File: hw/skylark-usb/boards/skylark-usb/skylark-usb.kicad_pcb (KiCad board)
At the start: 4 copper layers, 90 x 100 mm, 121 parts, among them J1 USB4105-GF-A, J2 BM08B-GHS-TBT, J3 20021111-00010T4LF, Q1 MMBFJ177LT1G, Q2 MMBFJ177LT1G, Q3 MMBFJ177LT1G, Q4 MMBFJ177LT1G, Q5 2N7002/HAMR, Q6 2N7002/HAMR, Q7 2N7002/HAMR, SW1 TL3342F160QG, SW2 TL3342F160QG, U1 STM32F072CBT6, U10 OPA387DBVR, U11 SHT40-AD1F-R2, U12 BMP390, U13 TPS22918DBVR, U2 AP2112K-3.3TRG1, U3 TPS2553DBVR, U4 REF3025AIDBZR, U5 OPA387DBVR, U6 ADS122C04IPWR, U7 OPA2387DGKR, U8 OPA387DBVR, U9 OPA2387DGKR

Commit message: Harden Skylark signal chain and add manufacturing audit
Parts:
- added C80: 100nF, Skylark:Capacitor_SMD__C_1206_3216Metric, B.Cu at (110.0, 85.5)
- added C81: 100nF, Skylark:Capacitor_SMD__C_1206_3216Metric, B.Cu at (110.0, 88.0)
- added C82: 100nF, Skylark:Capacitor_SMD__C_1206_3216Metric, B.Cu at (110.0, 90.5)
- added C83: 100nF, Skylark:Capacitor_SMD__C_1206_3216Metric, B.Cu at (110.0, 93.0)
- added C84: 100nF, Skylark:Capacitor_SMD__C_1206_3216Metric, B.Cu at (124.5, 81.5)
- added C85: 100nF, Skylark:Capacitor_SMD__C_1206_3216Metric, B.Cu at (124.5, 84.0)
- added C86: 100nF, Skylark:Capacitor_SMD__C_1206_3216Metric, B.Cu at (124.5, 86.5)
- added C87: 100nF, Skylark:Capacitor_SMD__C_1206_3216Metric, B.Cu at (124.5, 89.0)
- added D4: BAT54LT1G, Skylark:Package_TO_SOT_SMD__SOT-23, F.Cu at (56.0, 92.0)
- added R74: 10000R, Skylark:Resistor_SMD__R_0603_1608Metric, F.Cu at (67.0, 96.0)
- added R75: 100R, Skylark:Resistor_SMD__R_0603_1608Metric, F.Cu at (88.0, 96.0)
- C30, C33, C36, C56: footprint Skylark:Capacitor_SMD__C_0603_1608Metric -> Skylark:Capacitor_SMD__C_1206_3216Metric
- C50, C53: value 470nF -> 100nF; footprint Skylark:Capacitor_SMD__C_0603_1608Metric -> Skylark:Capacitor_SMD__C_1206_3216Metric
- Q1, Q2, Q3, Q4: value MMBFJ177LT1G -> MMBFJ270
- Q7: value 2N7002/HAMR -> MMBT3904LT1G
- R71: value 1e+06R -> 100000R
- moved C7 15.5 mm to (77.0, 127.8), turned to 180 degrees
- moved Q1 13.4 mm to (78.0, 68.0)
- moved Q3 13.4 mm to (120.0, 68.0)
- moved C9 10.7 mm to (86.8, 132.0), turned to -90 degrees
- moved C6 6.93 mm to (82.8, 118.0)
- moved C8 6.75 mm to (91.0, 122.2), turned to 0 degrees
- moved R4 6.32 mm to (110.0, 137.0), turned to -90 degrees
- moved C3 6.06 mm to (111.5, 132.1), turned to 180 degrees
- moved C4 4.23 mm to (120.5, 132.1), turned to 0 degrees
- moved Q4 4.12 mm to (130.0, 87.0)
- moved R3 4.00 mm to (120.0, 136.0)
- moved C10 3.64 mm to (79.5, 116.0), turned to 90 degrees
- moved C50 3.16 mm to (110.0, 83.0), turned to 180 degrees
- moved C1 2.99 mm to (57.5, 131.1), turned to 180 degrees
- moved C2 2.01 mm to (66.5, 131.1), turned to 0 degrees
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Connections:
- net 2 renamed u1-2
- Q7 pad 1: CLAMP_HOLD -> CLAMP_BASE
- Q7 pad 2: GND -> VZERO
- R70 pad 1: USB_5V -> GATE_SUPPLY
- R71 pad 2: GND -> VZERO
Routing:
- net GND: track 325.1 -> 92.4 mm, vias 77 -> 79
- net CLAMP_GATE: track 91.0 -> 134.6 mm, vias 2 -> 5
- net V3: track 291.6 -> 257.0 mm, vias 4 -> 2
- net PM_EN: track 46.8 -> 70.5 mm
- net H2S_WE_OUT: track 48.5 -> 68.8 mm, vias 3 -> 1
- net VZERO: track 114.1 -> 131.9 mm, vias 3 -> 4
- net H2S_AE_OUT: track 58.1 -> 73.7 mm, vias 3 -> 1
- net SO2_WE_OUT: track 86.6 -> 71.1 mm
- net PM_FAULT_N: track 65.7 -> 52.2 mm
- net H2S_WE_SUM: track 11.4 -> 23.6 mm
- net H2S_WE: track 23.4 -> 11.4 mm
- net H2S_AE_SUM: track 8.66 -> 19.6 mm
- net SO2_WE: track 20.8 -> 10.3 mm, vias 1 -> 0
- net NRST: track 78.2 -> 68.4 mm, vias 1 -> 2
- net VA: track 151.1 -> 141.6 mm
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- added copper zone on B.Cu, net GUARD
- added copper zone on F.Cu, net GUARD

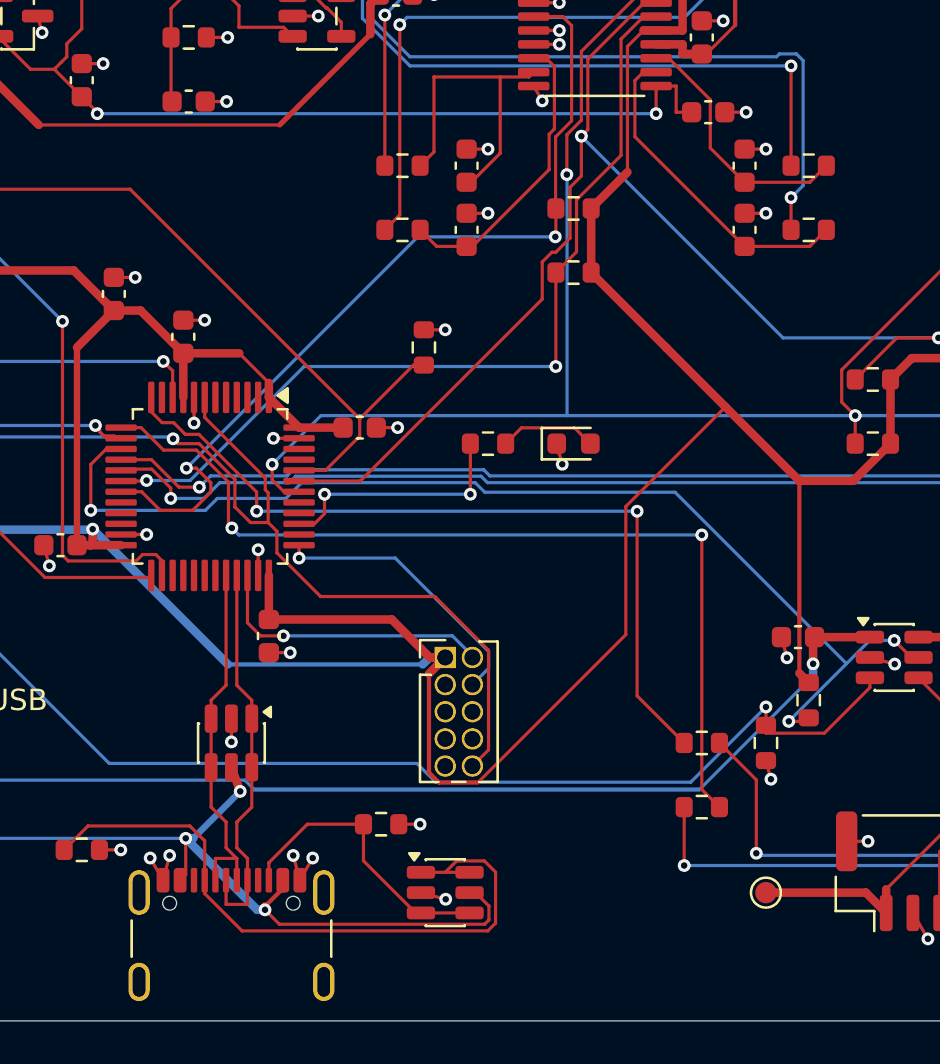
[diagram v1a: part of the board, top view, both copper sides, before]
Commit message: Finalize Skylark signal-chain updates and remove obsolete artifacts
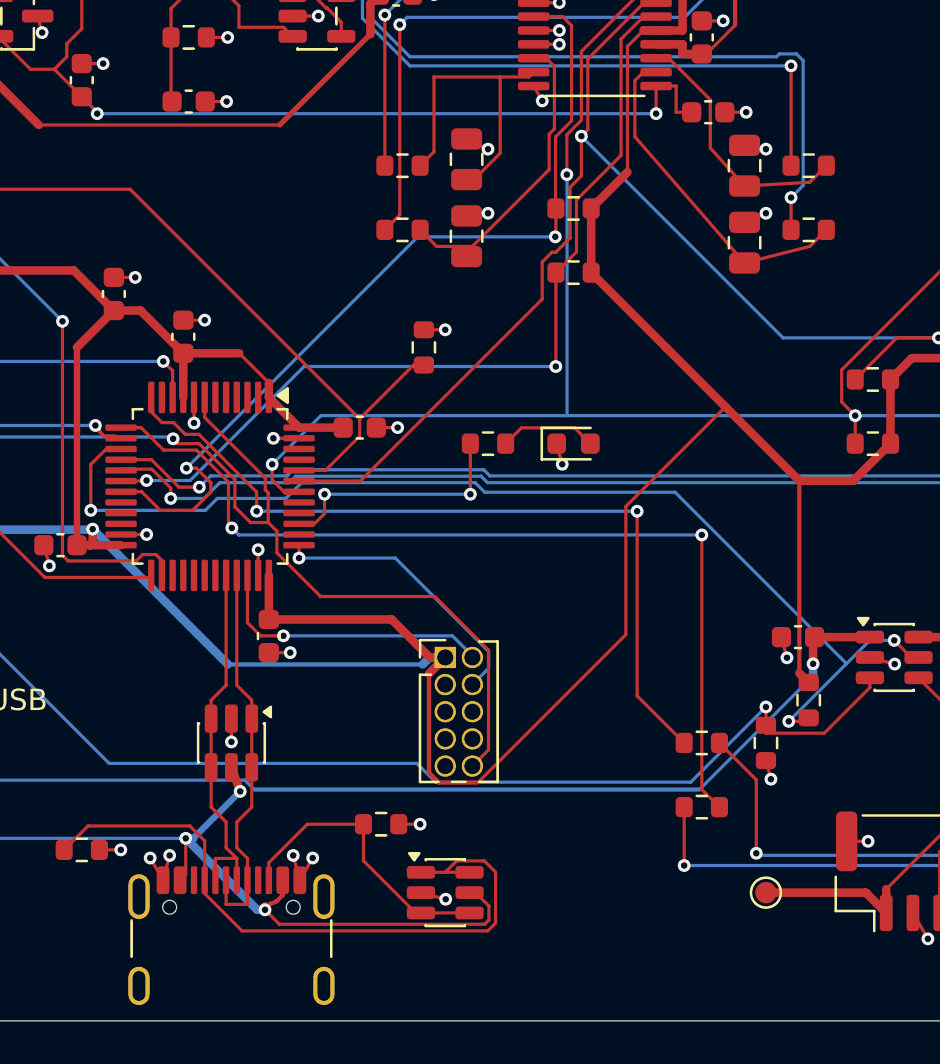
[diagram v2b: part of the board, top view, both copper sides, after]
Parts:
- C31, C34, C51, C54: value 1uF -> 10uF; footprint Skylark:Capacitor_SMD__C_0603_1608Metric -> Skylark:Capacitor_SMD__C_0805_2012Metric
- J1: value USB4105-GF-A -> TYPE-C-31-M-12; footprint Skylark:Connector_USB__USB_C_Receptacle_GCT_USB4105-xx-A_16P_TopMnt_Horizontal -> Skylark:USB_C_HRO_TYPE-C-31-M-12
- R3: value 80600R -> 82000R
- U12: value BMP390 -> BMP388; footprint Skylark:BMP390 -> Skylark:BMP388
- moved C34 0.60 mm to (109.0, 113.6)
- moved C51 0.30 mm to (96.0, 109.7)
- moved C54 0.30 mm to (96.0, 113.3)
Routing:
- net SO2_AE_ADC: track 15.2 -> 15.8 mm
